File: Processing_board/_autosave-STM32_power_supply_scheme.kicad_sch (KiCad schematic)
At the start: 14 parts

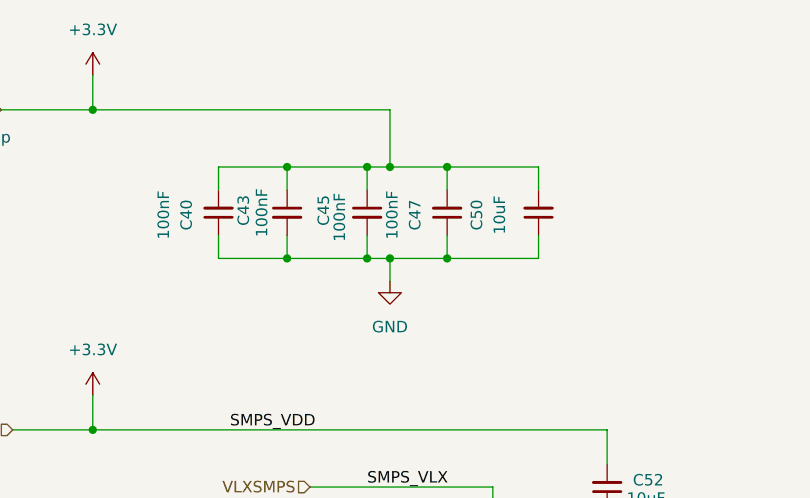
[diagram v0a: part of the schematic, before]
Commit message: had to rename all components on the PCB to match the schematic
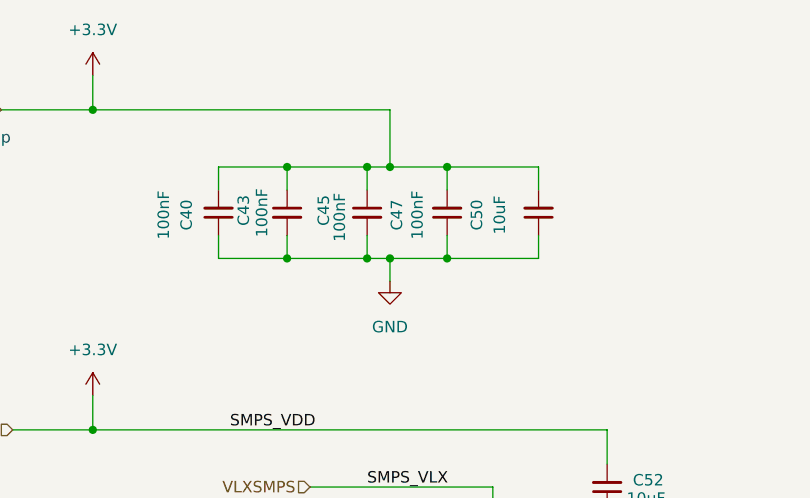
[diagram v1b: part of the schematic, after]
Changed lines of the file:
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@@
 		(dnp no)
 		(property "Reference" "C47"
-			(at 119.634 39.624 90)
+			(at 117.602 39.624 90)
 			(effects
 				(font
@@
 		)
 		(property "Value" "100nF"
-			(at 117.094 39.624 90)
+			(at 119.888 39.624 90)
 			(effects
 				(font
